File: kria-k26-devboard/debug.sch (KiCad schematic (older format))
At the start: 69 parts, among them J7 0878311420, Q5 BSS138-7-F, Q6 BSS138-7-F, Q7 BSS138-7-F, U23 FT4232HPQ, U35 93LC56CT-IMC, U36 SN74AVC2T245RSWR, U37 SN74AVC2T245RSWR, U38 SN74AVC4T245PWR, U39 SN74AVC4T245PWR, U40 NC7WZ07P6X, Y2 ABM8G-12.000MHZ-18-D2Y-T

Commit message: Initial placement of power supply
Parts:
- gave numbers to parts that had none: 13
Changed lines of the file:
@@
 USB_3V3
 $Comp
-L antmicroPMICVoltageRegulatorsLinear:MCP1799-3302H_DB U?
+L antmicroPMICVoltageRegulatorsLinear:MCP1799-3302H_DB U47
 U 1 1 65A4658C
 P 4150 1250
-F 0 "U?" H 4150 1537 60  0000 C CNN
+F 0 "U47" H 4150 1537 60  0000 C CNN
 F 1 "MCP1799-3302H_DB" H 4150 1431 60  0000 C CNN
 F 2 "antmicro-footprints:SOT-223" H 4350 700 60  0001 L CNN
@@
 PD_3V3
 $Comp
-L antmicroCapacitors0603:C_10u_0603 C?
+L antmicroCapacitors0603:C_10u_0603 C203
 U 1 1 65B0DD60
 P 4950 1500
-F 0 "C?" H 5065 1545 60  0000 L CNN
+F 0 "C203" H 5065 1545 60  0000 L CNN
 F 1 "C_10u_0603" H 4950 1350 60  0001 C CNN
 F 2 "antmicro-footprints:0603-cap" H 5150 1700 60  0001 L CNN
@@
 AR Path="/63C44BC2/623E44F4/65B0DD6D" Ref="C?"  Part="1"
 AR Path="/63C44BC2/6244F9D5/65B0DD6D" Ref="C?"  Part="1"
-AR Path="/625B0244/65B0DD6D" Ref="C?"  Part="1"
-F 0 "C?" H 3600 1350 60  0000 C CNN
+AR Path="/625B0244/65B0DD6D" Ref="C201"  Part="1"
+F 0 "C201" H 3600 1350 60  0000 C CNN
 F 1 "C_100n_0402" H 3500 1300 60  0001 C CNN
 F 2 "antmicro-footprints:0402-cap" H 3700 1650 60  0001 L CNN
@@
 AR Path="/63C44BC2/623E44F4/65B0DD77" Ref="#PWR?"  Part="1"
 AR Path="/63C44BC2/6244F9D5/65B0DD77" Ref="#PWR?"  Part="1"
-AR Path="/625B0244/65B0DD77" Ref="#PWR?"  Part="1"
-F 0 "#PWR?" H 3500 1400 50  0001 C CNN
+AR Path="/625B0244/65B0DD77" Ref="#PWR0360"  Part="1"
+F 0 "#PWR0360" H 3500 1400 50  0001 C CNN
 F 1 "GND" H 3505 1477 50  0000 C CNN
 F 2 "" H 3500 1650 50  0001 C CNN
@@
 AR Path="/63C44BC2/623E44F4/65B0DD81" Ref="#PWR?"  Part="1"
 AR Path="/63C44BC2/6244F9D5/65B0DD81" Ref="#PWR?"  Part="1"
-AR Path="/625B0244/65B0DD81" Ref="#PWR?"  Part="1"
-F 0 "#PWR?" H 4150 1400 50  0001 C CNN
+AR Path="/625B0244/65B0DD81" Ref="#PWR0361"  Part="1"
+F 0 "#PWR0361" H 4150 1400 50  0001 C CNN
 F 1 "GND" H 4155 1477 50  0000 C CNN
 F 2 "" H 4150 1650 50  0001 C CNN
@@
 AR Path="/63C44BC2/623E44F4/65B0DD8B" Ref="#PWR?"  Part="1"
 AR Path="/63C44BC2/6244F9D5/65B0DD8B" Ref="#PWR?"  Part="1"
-AR Path="/625B0244/65B0DD8B" Ref="#PWR?"  Part="1"
-F 0 "#PWR?" H 4950 1400 50  0001 C CNN
+AR Path="/625B0244/65B0DD8B" Ref="#PWR0362"  Part="1"
+F 0 "#PWR0362" H 4950 1400 50  0001 C CNN
 F 1 "GND" H 4955 1477 50  0000 C CNN
 F 2 "" H 4950 1650 50  0001 C CNN
@@
 USBC_VBUS
 $Comp
-L antmicroResistors0402:R_0R_0402 R?
+L antmicroResistors0402:R_0R_0402 R116
 U 1 1 65D83F07
 P 2850 10650
-F 0 "R?" H 2850 10750 60  0000 C CNN
+F 0 "R116" H 2850 10750 60  0000 C CNN
 F 1 "R_0R_0402" H 2850 10500 60  0001 C CNN
 F 2 "antmicro-footprints:0402-res" H 3050 10850 60  0001 L CNN
@@
 $EndComp
 $Comp
-L antmicroResistors0402:R_0R_0402 R?
+L antmicroResistors0402:R_0R_0402 R113
 U 1 1 65D84532
 P 2050 10450
-F 0 "R?" H 2050 10550 60  0000 C CNN
+F 0 "R113" H 2050 10550 60  0000 C CNN
 F 1 "R_0R_0402" H 2050 10300 60  0001 C CNN
 F 2 "antmicro-footprints:0402-res" H 2250 10650 60  0001 L CNN
@@
 USB_N
 $Comp
-L antmicroUSBDVIHDMIConnectors:10103594-0001LF J?
+L antmicroUSBDVIHDMIConnectors:10103594-0001LF J11
 U 1 1 65FE35F4
 P 1350 2000
-F 0 "J?" H 1364 2723 50  0000 C CNN
+F 0 "J11" H 1364 2723 50  0000 C CNN
 F 1 "10103594-0001LF" H 1364 2632 50  0000 C CNN
 F 2 "antmicro-footprints:USB_Micro_B_Female_10103594-0001LF" H 1550 2200 60  0001 L CNN
@@
 AR Path="/63C44BC2/623E44F4/6602D48C" Ref="#PWR?"  Part="1"
 AR Path="/63C44BC2/6244F9D5/6602D48C" Ref="#PWR?"  Part="1"
-AR Path="/625B0244/6602D48C" Ref="#PWR?"  Part="1"
-F 0 "#PWR?" H 1700 2000 50  0001 C CNN
+AR Path="/625B0244/6602D48C" Ref="#PWR0363"  Part="1"
+F 0 "#PWR0363" H 1700 2000 50  0001 C CNN
 F 1 "GND" H 1705 2077 50  0000 C CNN
 F 2 "" H 1700 2250 50  0001 C CNN
@@
 AR Path="/63C44BC2/623E44F4/66051E26" Ref="#PWR?"  Part="1"
 AR Path="/63C44BC2/6244F9D5/66051E26" Ref="#PWR?"  Part="1"
-AR Path="/625B0244/66051E26" Ref="#PWR?"  Part="1"
-F 0 "#PWR?" H 1200 2450 50  0001 C CNN
+AR Path="/625B0244/66051E26" Ref="#PWR0364"  Part="1"
+F 0 "#PWR0364" H 1200 2450 50  0001 C CNN
 F 1 "GND" H 1205 2527 50  0000 C CNN
 F 2 "" H 1200 2700 50  0001 C CNN
@@
 	7000 8200 7050 8200
 $Comp
-L antmicroResistors0402:R_0R_0402 R?
+L antmicroResistors0402:R_0R_0402 R112
 U 1 1 6615CA96
 P 2050 10250
-F 0 "R?" H 2050 10350 60  0000 C CNN
+F 0 "R112" H 2050 10350 60  0000 C CNN
 F 1 "R_0R_0402" H 2050 10100 60  0001 C CNN
 F 2 "antmicro-footprints:0402-res" H 2250 10450 60  0001 L CNN
@@
 USBC_N
 $Comp
-L antmicroResistors0402:R_0R_0402 R?
+L antmicroResistors0402:R_0R_0402 R114
 U 1 1 65DA954B
 P 2050 10650
-F 0 "R?" H 2050 10750 60  0000 C CNN
+F 0 "R114" H 2050 10750 60  0000 C CNN
 F 1 "R_0R_0402" H 2050 10500 60  0001 C CNN
 F 2 "antmicro-footprints:0402-res" H 2250 10850 60  0001 L CNN
@@
 $EndComp
 $Comp
-L antmicroResistors0402:R_0R_0402 R?
+L antmicroResistors0402:R_0R_0402 R115
 U 1 1 65DA9332
 P 2850 10450
-F 0 "R?" H 2850 10550 60  0000 C CNN
+F 0 "R115" H 2850 10550 60  0000 C CNN
 F 1 "R_0R_0402" H 2850 10300 60  0001 C CNN
 F 2 "antmicro-footprints:0402-res" H 3050 10650 60  0001 L CNN
@@
 USB_3V3
 $Comp
-L antmicroPMICVoltageRegulatorsLinear:MCP1799-3302H_DB U?
+L antmicroPMICVoltageRegulatorsLinear:MCP1799-3302H_DB U48
 U 1 1 667265D6
 P 4150 2500
-F 0 "U?" H 4150 2787 60  0000 C CNN
+F 0 "U48" H 4150 2787 60  0000 C CNN
 F 1 "MCP1799-3302H_DB" H 4150 2681 60  0000 C CNN
 F 2 "antmicro-footprints:SOT-223" H 4350 1950 60  0001 L CNN
@@
 $EndComp
 $Comp
-L antmicroCapacitors0603:C_10u_0603 C?
+L antmicroCapacitors0603:C_10u_0603 C204
 U 1 1 66726B02
 P 4950 2750
-F 0 "C?" H 5065 2795 60  0000 L CNN
+F 0 "C204" H 5065 2795 60  0000 L CNN
 F 1 "C_10u_0603" H 4950 2600 60  0001 C CNN
 F 2 "antmicro-footprints:0603-cap" H 5150 2950 60  0001 L CNN
@@
 AR Path="/63C44BC2/623E44F4/66726B0F" Ref="C?"  Part="1"
 AR Path="/63C44BC2/6244F9D5/66726B0F" Ref="C?"  Part="1"
-AR Path="/625B0244/66726B0F" Ref="C?"  Part="1"
-F 0 "C?" H 3600 2600 60  0000 C CNN
+AR Path="/625B0244/66726B0F" Ref="C202"  Part="1"
+F 0 "C202" H 3600 2600 60  0000 C CNN
 F 1 "C_100n_0402" H 3500 2550 60  0001 C CNN
 F 2 "antmicro-footprints:0402-cap" H 3700 2900 60  0001 L CNN
@@
 AR Path="/63C44BC2/623E44F4/66726B19" Ref="#PWR?"  Part="1"
 AR Path="/63C44BC2/6244F9D5/66726B19" Ref="#PWR?"  Part="1"
-AR Path="/625B0244/66726B19" Ref="#PWR?"  Part="1"
-F 0 "#PWR?" H 3500 2650 50  0001 C CNN
+AR Path="/625B0244/66726B19" Ref="#PWR0365"  Part="1"
+F 0 "#PWR0365" H 3500 2650 50  0001 C CNN
 F 1 "GND" H 3505 2727 50  0000 C CNN
 F 2 "" H 3500 2900 50  0001 C CNN
@@
 AR Path="/63C44BC2/623E44F4/66726B23" Ref="#PWR?"  Part="1"
 AR Path="/63C44BC2/6244F9D5/66726B23" Ref="#PWR?"  Part="1"
-AR Path="/625B0244/66726B23" Ref="#PWR?"  Part="1"
-F 0 "#PWR?" H 4150 2650 50  0001 C CNN
+AR Path="/625B0244/66726B23" Ref="#PWR0366"  Part="1"
+F 0 "#PWR0366" H 4150 2650 50  0001 C CNN
 F 1 "GND" H 4155 2727 50  0000 C CNN
 F 2 "" H 4150 2900 50  0001 C CNN
@@
 AR Path="/63C44BC2/623E44F4/66726B2D" Ref="#PWR?"  Part="1"
 AR Path="/63C44BC2/6244F9D5/66726B2D" Ref="#PWR?"  Part="1"
-AR Path="/625B0244/66726B2D" Ref="#PWR?"  Part="1"
-F 0 "#PWR?" H 4950 2650 50  0001 C CNN
+AR Path="/625B0244/66726B2D" Ref="#PWR0367"  Part="1"
+F 0 "#PWR0367" H 4950 2650 50  0001 C CNN
 F 1 "GND" H 4955 2727 50  0000 C CNN
 F 2 "" H 4950 2900 50  0001 C CNN
@@
 Connection ~ 4150 2850
 $Comp
-L antmicroResistors0402:R_100k_0402 R?
+L antmicroResistors0402:R_100k_0402 R117
 U 1 1 66B3994C
 P 12250 9350
-F 0 "R?" V 12205 9420 60  0000 L CNN
+F 0 "R117" V 12205 9420 60  0000 L CNN
 F 1 "R_100k_0402" H 12250 9200 60  0001 C CNN
 F 2 "antmicro-footprints:0402-res" H 12450 9550 60  0001 L CNN

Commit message: Progress in PCB placement
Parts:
- removed J11: 10103594-0001LF, antmicro-footprints:USB_Micro_B_Female_10103594-0001LF, symbol antmicroUSBDVIHDMIConnectors:10103594-0001LF
- added J8: 1050170001, antmicro-footprints:USB_Micro_B_Female_1050170001, symbol antmicroUSBDVIHDMIConnectors:1050170001
- U32: renamed from U38; footprint Package_SO:TSSOP-16_4.4x5mm_P0.65mm -> antmicro-footprints:TSSOP-16_4.4x5mm_P0.65mm
- U33: renamed from U39; footprint Package_SO:TSSOP-16_4.4x5mm_P0.65mm -> antmicro-footprints:TSSOP-16_4.4x5mm_P0.65mm
- renumbered C157 to C125, C159 to C126, C160 to C127, C161 to C128, C162 to C129, C163 to C130, C164 to C131, C165 to C132, C166 to C133, C167 to C134, C168 to C135, C169 to C136, C170 to C137, C171 to C138, C201 to C139, C202 to C140, C176 to C141, C203 to C142, C204 to C143, C178 to C144, C174 to C145, C172 to C146, C188 to C147, C181 to C148, C182 to C149, C179 to C150, C180 to C151, C184 to C152, C183 to C153, C185 to C154, C186 to C155, C187 to C156, FB1 to FB3, FB2 to FB4, FB3 to FB5, J7 to J9, Q7 to Q10, Q5 to Q11, Q6 to Q9, R112 to R78, R113 to R79, R114 to R80, R115 to R81, R116 to R82, R80 to R83, R81 to R84, R72 to R85, R73 to R86, R82 to R87, R76 to R88, R77 to R89, R78 to R90, R86 to R91, R79 to R92, R87 to R93, R117 to R94, R84 to R95, R85 to R96, U47 to U28, U48 to U29, U23 to U30, U35 to U31, U36 to U34, U37 to U35, U40 to U36, Y2 to Y5

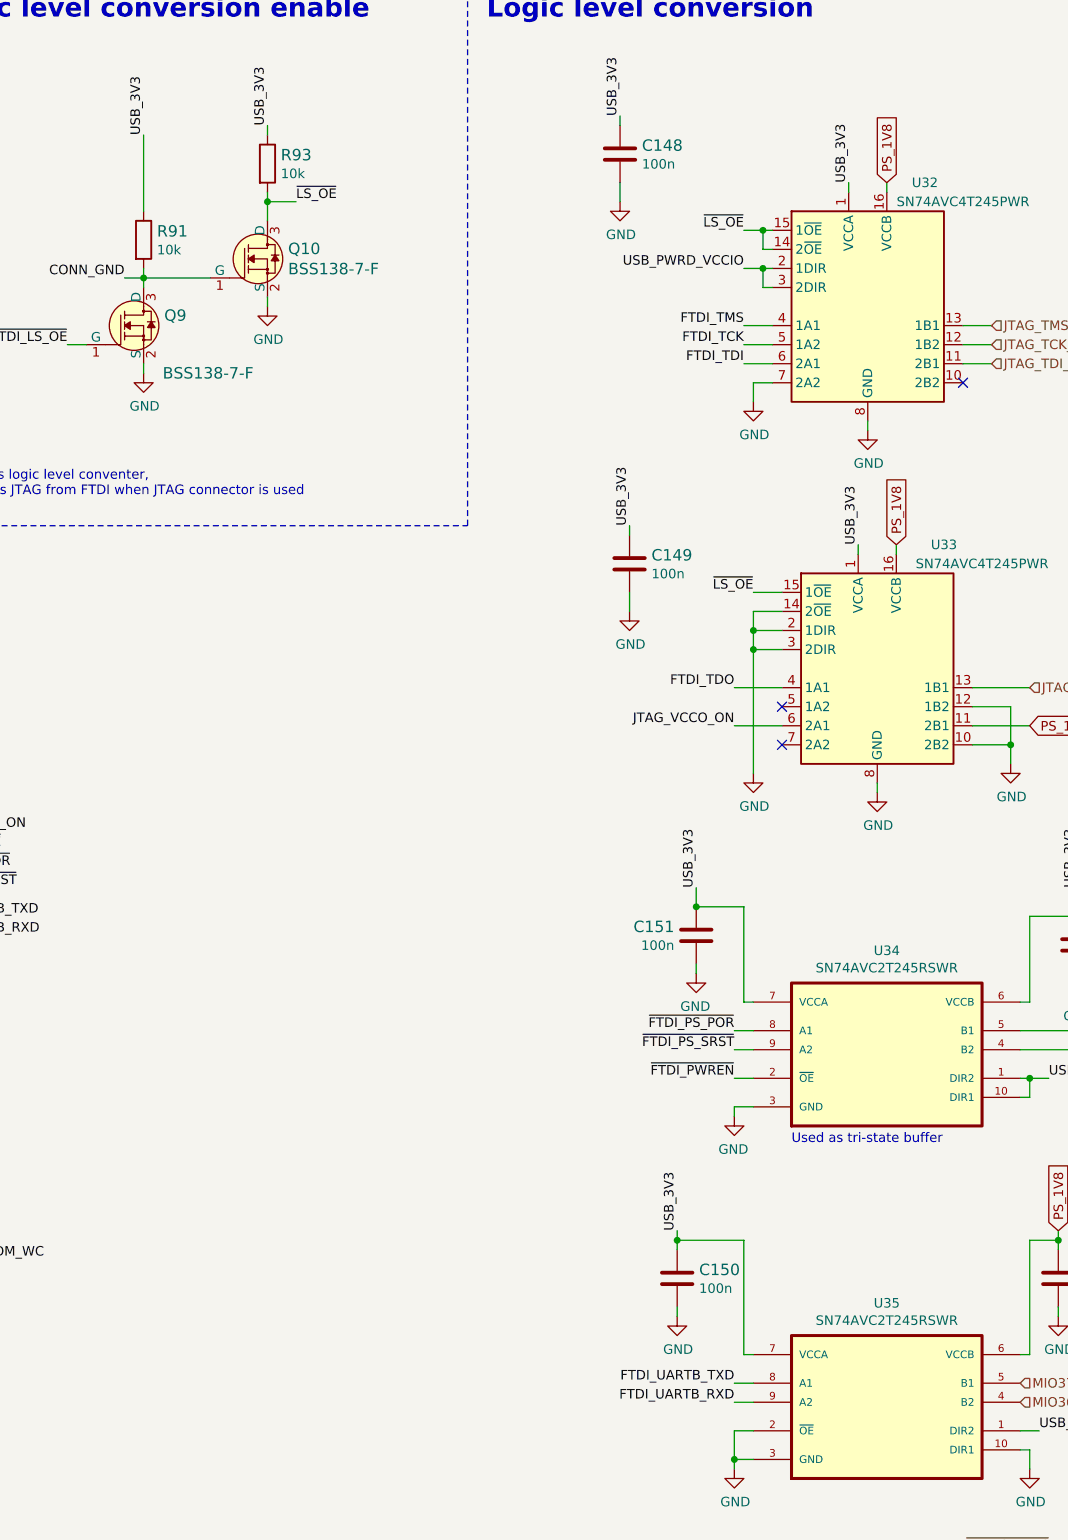
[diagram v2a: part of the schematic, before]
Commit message: Added logic level direction marking for better clarity
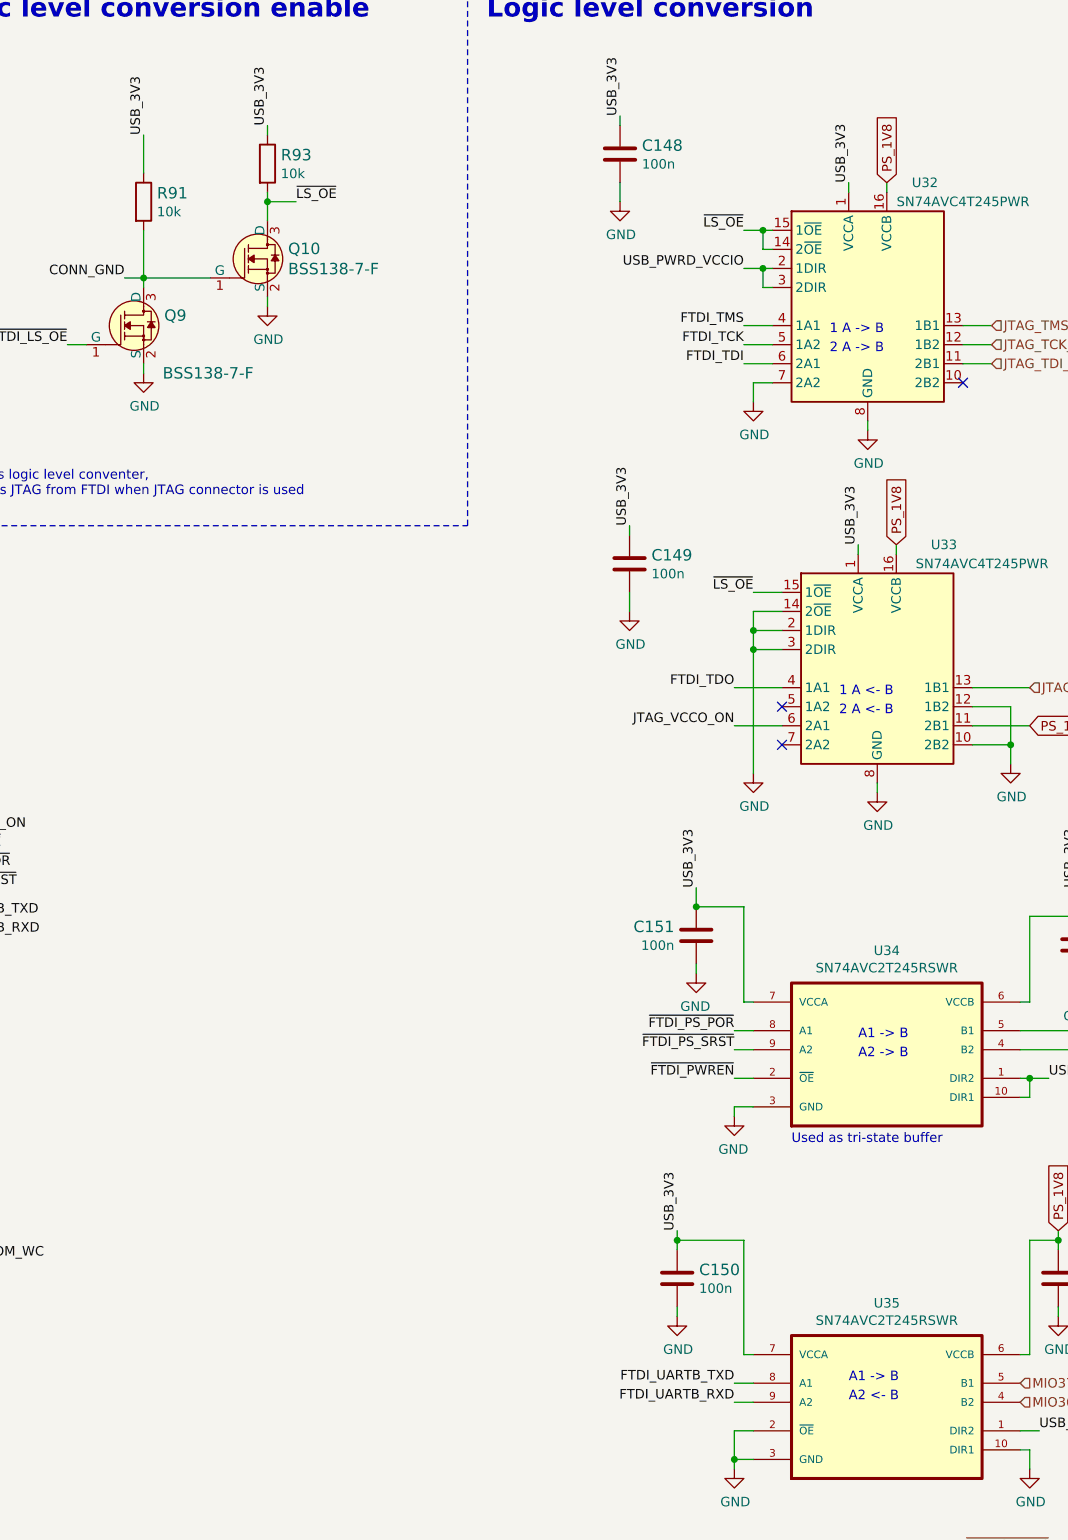
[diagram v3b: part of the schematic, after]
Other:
- note added: "1 A -> B"
- note added: "1 A <- B"
- note added: "2 A -> B"
- note added: "2 A <- B"
- note added: "A1 -> B"
- note added: "A2 -> B"
- note added: "A2 <- B"
- moved on the sheet: R91
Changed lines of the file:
@@
 L antmicroResistors0402:R_10k_0402 R91
 U 1 1 623BF93A
-P 8550 1850
-F 0 "R91" V 8505 1920 60  0000 L CNN
-F 1 "R_10k_0402" H 8550 1700 60  0001 C CNN
-F 2 "antmicro-footprints:0402-res" H 8750 2050 60  0001 L CNN
-F 3 "" H 8550 1850 50  0001 C CNN
-F 4 "VISHAY" H 8750 2250 60  0001 L CNN "Manufacturer"
-F 5 "CRCW040210K0FKEDHP" H 8750 2150 60  0001 L CNN "MPN"
-F 6 "10k" V 8603 1920 50  0000 L CNN "Val"
-	1    8550 1850
+P 8550 1650
+F 0 "R91" V 8505 1720 60  0000 L CNN
+F 1 "R_10k_0402" H 8550 1500 60  0001 C CNN
+F 2 "antmicro-footprints:0402-res" H 8750 1850 60  0001 L CNN
+F 3 "" H 8550 1650 50  0001 C CNN
+F 4 "VISHAY" H 8750 2050 60  0001 L CNN "Manufacturer"
+F 5 "CRCW040210K0FKEDHP" H 8750 1950 60  0001 L CNN "MPN"
+F 6 "10k" V 8603 1720 50  0000 L CNN "Val"
+	1    8550 1650
 	0    1    1    0
 $EndComp
@@
 Connection ~ 8550 2050
 Wire Wire Line
-	8550 2050 8550 2000
+	8550 2050 8550 1800
 $Comp
 L power:GND #PWR0319
@@
 	9200 2200 9200 2150
 Wire Wire Line
-	8550 1300 8550 1700
+	8550 1300 8550 1500
 Wire Wire Line
 	9200 1300 9200 1250
@@
 	1    0    0    -1
 $EndComp
+Text Notes 12200 4350 0    50   ~ 0
+2 A <- B
+Text Notes 12150 2350 0    50   ~ 0
+1 A -> B
+Text Notes 12150 2450 0    50   ~ 0
+2 A -> B
+Text Notes 12200 4250 0    50   ~ 0
+1 A <- B
+Text Notes 12300 6050 0    50   ~ 0
+A1 -> B
+Text Notes 12300 6150 0    50   ~ 0
+A2 -> B
+Text Notes 12250 7850 0    50   ~ 0
+A1 -> B
+Text Notes 12250 7950 0    50   ~ 0
+A2 <- B
 Wire Bus Line
 	4700 6500 4700 6700
